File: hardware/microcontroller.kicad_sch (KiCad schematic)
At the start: 12 parts, among them J1 AVR-ISP-6, SW1 SW_Push_Open_Dual, U1 ATmega328P-A, Y1 Crystal

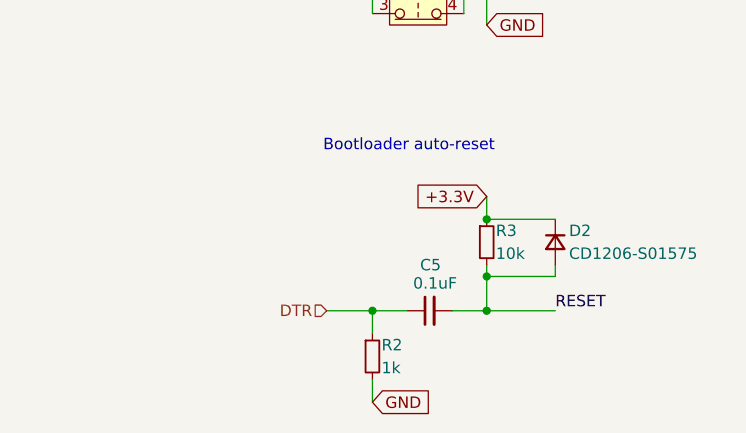
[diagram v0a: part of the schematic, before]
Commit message: Minor cosmetic changes
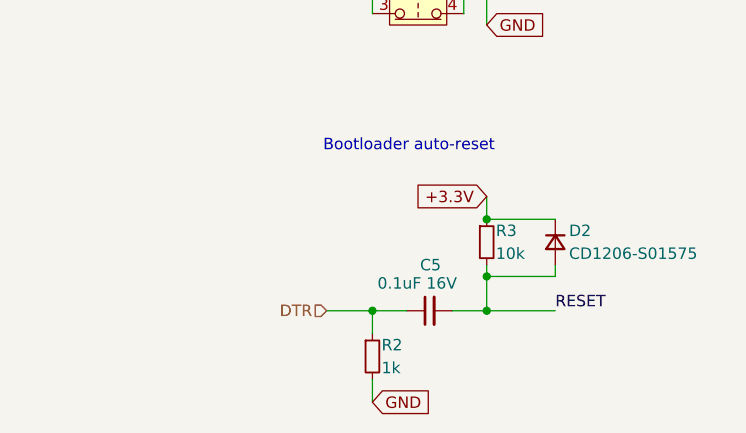
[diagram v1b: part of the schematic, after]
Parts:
- C5: value 0.1uF -> 0.1uF 16V; Package (none) -> 0805; Part Num (none) -> GRM21BR71H104KA01L; Price/unit (none) -> $0.0097; Supplier Link (none) -> https://jlcpcb.com/partdetail/MurataElectronics-GRM21BR71H1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
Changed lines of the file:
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@@
 			)
 		)
-		(property "Value" "0.1uF"
+		(property "Value" "0.1uF 16V"
 			(at 239.268 134.112 90)
 			(effects
@@
 			)
 		)
-		(property "Datasheet" "~"
+		(property "Datasheet" "https://wmsc.lcsc.com/wmsc/upload/file/pdf/v2/lcsc/2304140030_Murata-Electronics-GRM21BR71H104KA01L_C77082.pdf"
 			(at 236.22 137.16 0)
 			(effects
@@
 			(at 236.22 137.16 0)
 			(effects
+				(font
+					(size 1.27 1.27)
+				)
+				(hide yes)
+			)
+		)
+		(property "Package" "0805"
+			(at 236.22 137.16 0)
+			(effects
+				(font
+					(size 1.27 1.27)
+				)
+				(hide yes)
+			)
+		)
+		(property "Part Num" "GRM21BR71H104KA01L"
+			(at 236.22 137.16 0)
+			(effects
+				(font
+					(size 1.27 1.27)
+				)
+				(hide yes)
+			)
+		)
+		(property "Price/unit" "$0.0097"
+			(at 236.22 137.16 0)
+			(effects
+				(font
+					(size 1.27 1.27)
+				)
+				(hide yes)
+			)
+		)
+		(property "Supplier Link" "https://jlcpcb.com/partdetail/MurataElectronics-GRM21BR71H104KA01L/C77082"
+			(at 236.22 137.16 0)
+			(effects

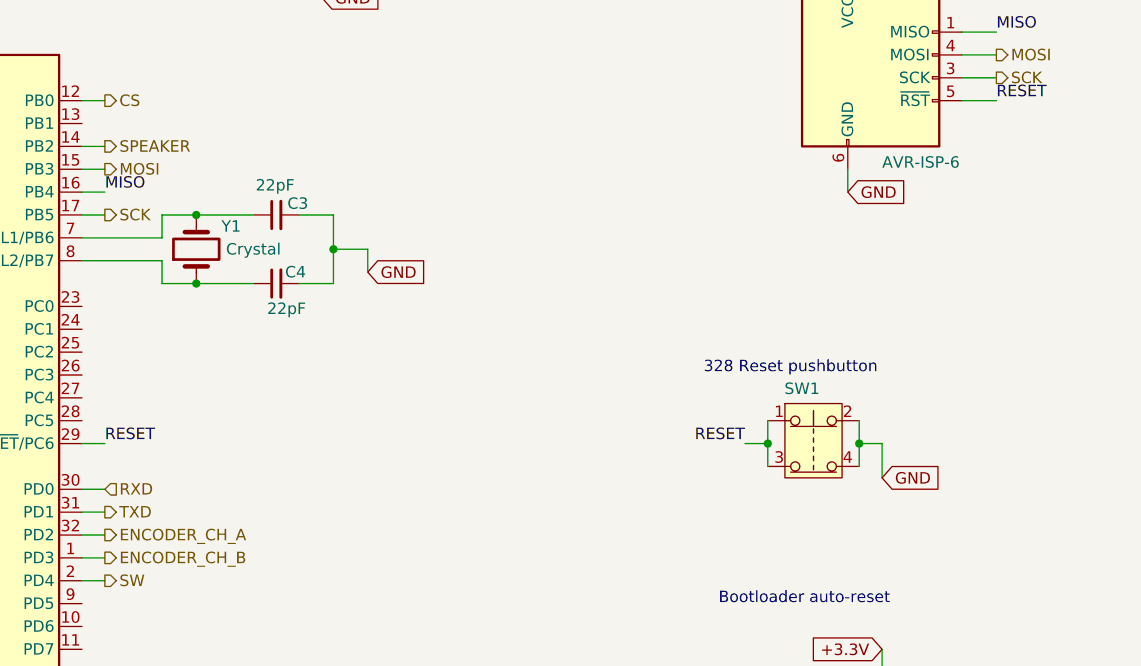
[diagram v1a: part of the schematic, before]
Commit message: Added information, footprints and 3d models for several components
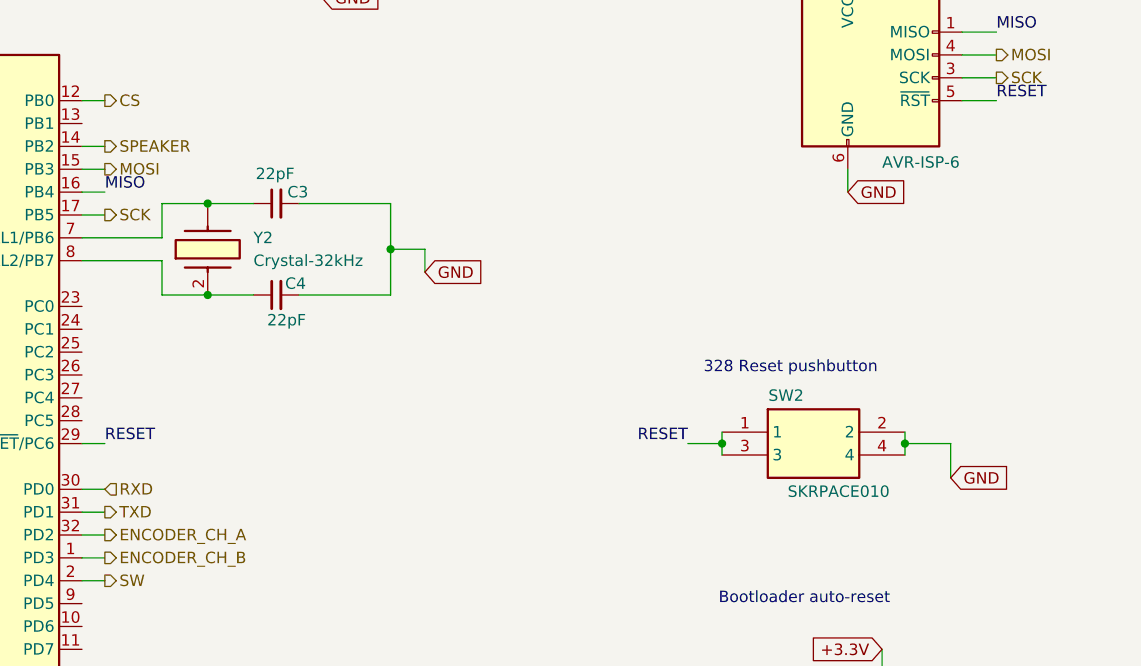
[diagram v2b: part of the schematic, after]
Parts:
- removed SW1: SW_Push_Open_Dual, symbol Switch:SW_Push_Open_Dual
- removed Y1: Crystal, symbol Device:Crystal
- added SW2: SKRPACE010, SMT(4.2X3.2), symbol kitchen_timer-symbols_lib:SKRPACE010
- added Y2: Crystal-32kHz, kitchen_timer:FL26T2-32.000, symbol kitchen_timer-symbols_lib:FL26T2-32.000
- U1: Package (none) -> TQFP-32(7x7); Part Num (none) -> ATMEGA328P-AU; Price/unit (none) -> $2.2845; Supplier Link (none) -> https://jlcpcb.com/partdetail/MicrochipTech-ATMEGA328PAU/C1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
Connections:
- net GND: now also SW2.2, SW2.4
- net RESET: now also SW2.1, SW2.3
- net at C4.1, U1.8 (XTAL2/PB7): now also Y2.2 (CRYSTAL_2)
- net at C3.1, U1.7 (XTAL1/PB6): now also Y2.
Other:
- moved on the sheet: C3, C4

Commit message: Added some information to the microcontroller sch and the power_management sch
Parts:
- SW2: Package (none) -> SMD; Part Num (none) -> SKRPACE010; Price/unit (none) -> $0.0573; Supplier Link (none) -> https://jlcpcb.com/partdetail/Alpsalpine-SKRPACE010/C139797
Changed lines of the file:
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@@
 			)
 		)
-		(property "Datasheet" "http://www.alps.com/prod/info/E/HTML/Tact/SurfaceMount/SKRP/SKRPACE010.html"
+		(property "Datasheet" "https://www.lcsc.com/datasheet/lcsc_datasheet_1811051610_ALPSALPINE-SKRPACE010_C139797.pdf"
 			(at 241.3 295.25 0)
 			(effects
@@
 				(hide yes)
 			)
+		)
+		(property "Supplier Link" "https://jlcpcb.com/partdetail/Alpsalpine-SKRPACE010/C139797"
+			(at 224.79 100.33 0)
+			(effects
+				(font
+					(size 1.27 1.27)
+				)
+				(hide yes)
+			)
+		)
+		(property "Price/unit" " $0.0573"
+			(at 224.79 100.33 0)
+			(effects
+				(font
+					(size 1.27 1.27)
+				)
+				(hide yes)
+			)
+		)
+		(property "Part Num" "SKRPACE010"
+			(at 224.79 100.33 0)
+			(effects
+				(font
+					(size 1.27 1.27)
+				)
+				(hide yes)
+			)
+		)
+		(property "Package" "SMD"
+			(at 224.79 100.33 0)
+			(effects
+				(font
+					(size 1.27 1.27)
+				)
+				(hide yes)
+			)

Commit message: Added TP4056 footprint andconfirmed components in UART and BMS schematics.
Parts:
- SW2: footprint SMT(4.2X3.2) -> (none)
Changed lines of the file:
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@@
 			)
 		)
-		(property "Footprint" "SMT(4.2X3.2)"
+		(property "Footprint" ""
 			(at 241.3 195.25 0)
 			(effects

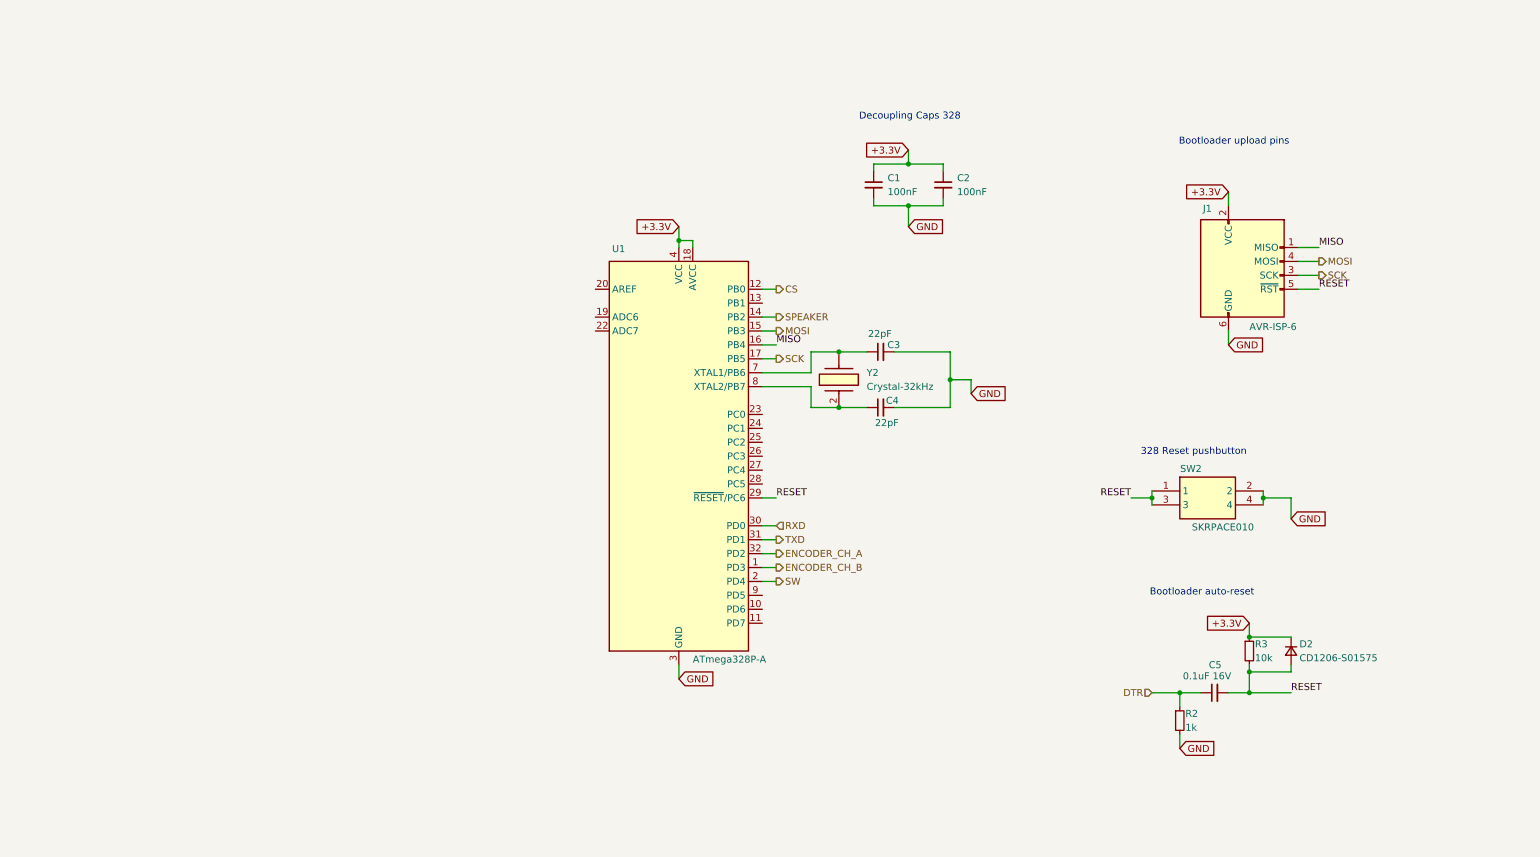
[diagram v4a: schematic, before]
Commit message: Removed the 3.3V Regulator since we might need to run everything out of 5V
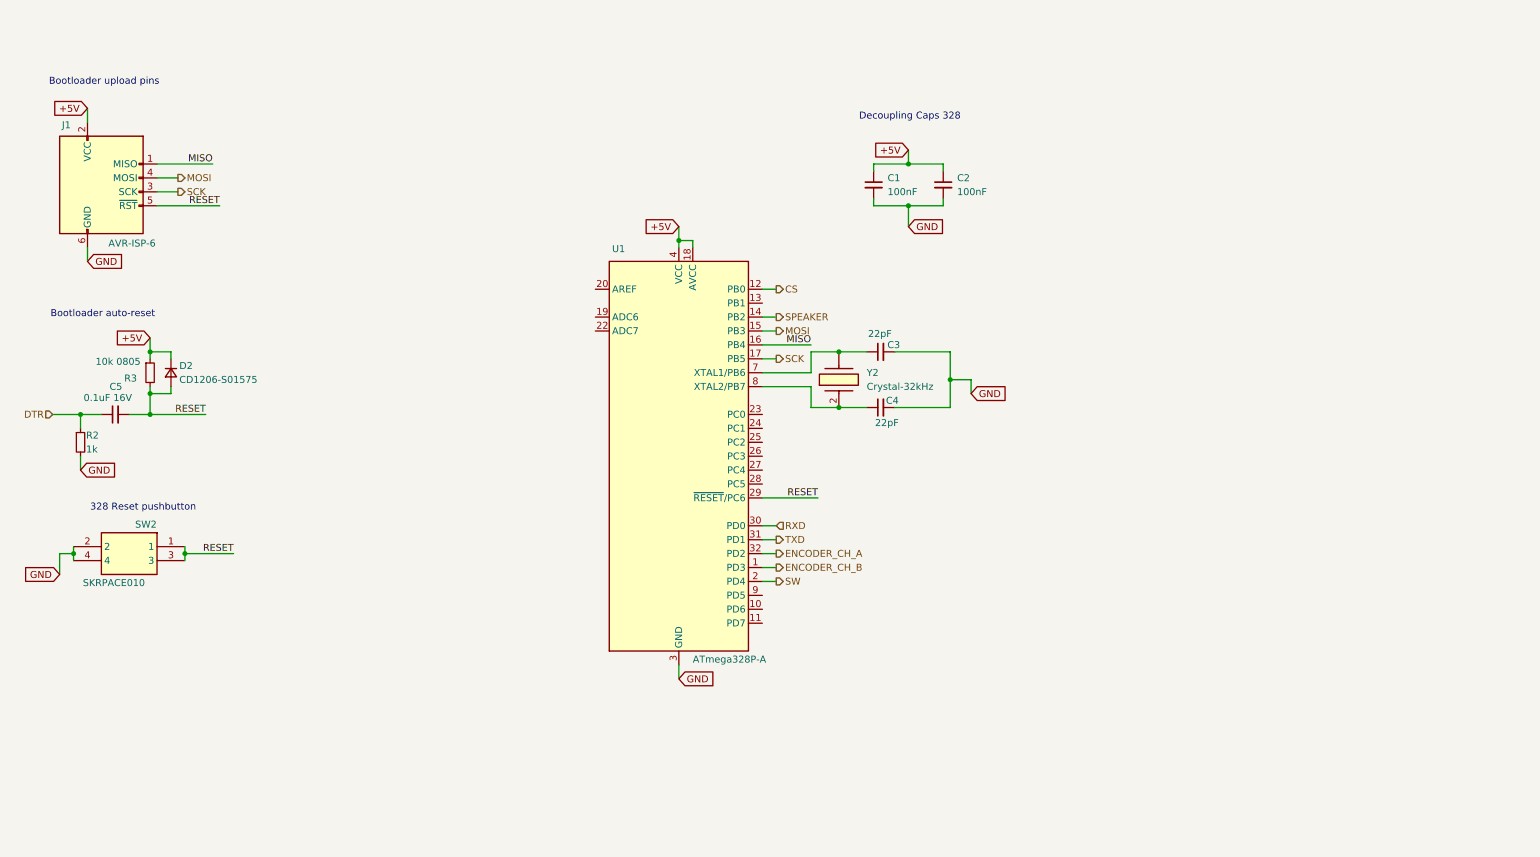
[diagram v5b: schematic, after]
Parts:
- R3: value 10k -> 10k 0805; Package (none) -> 0805; Part Num (none) -> 0805W8F1002T5E; Price/unit (none) -> $0.0017; Supplier Link (none) -> https://jlcpcb.com/partdetail/18102-0805W8F1002T5E/C17414
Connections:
- net +3.3V renamed +5V
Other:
- moved on the sheet: C5, D2, J1, R2, SW2

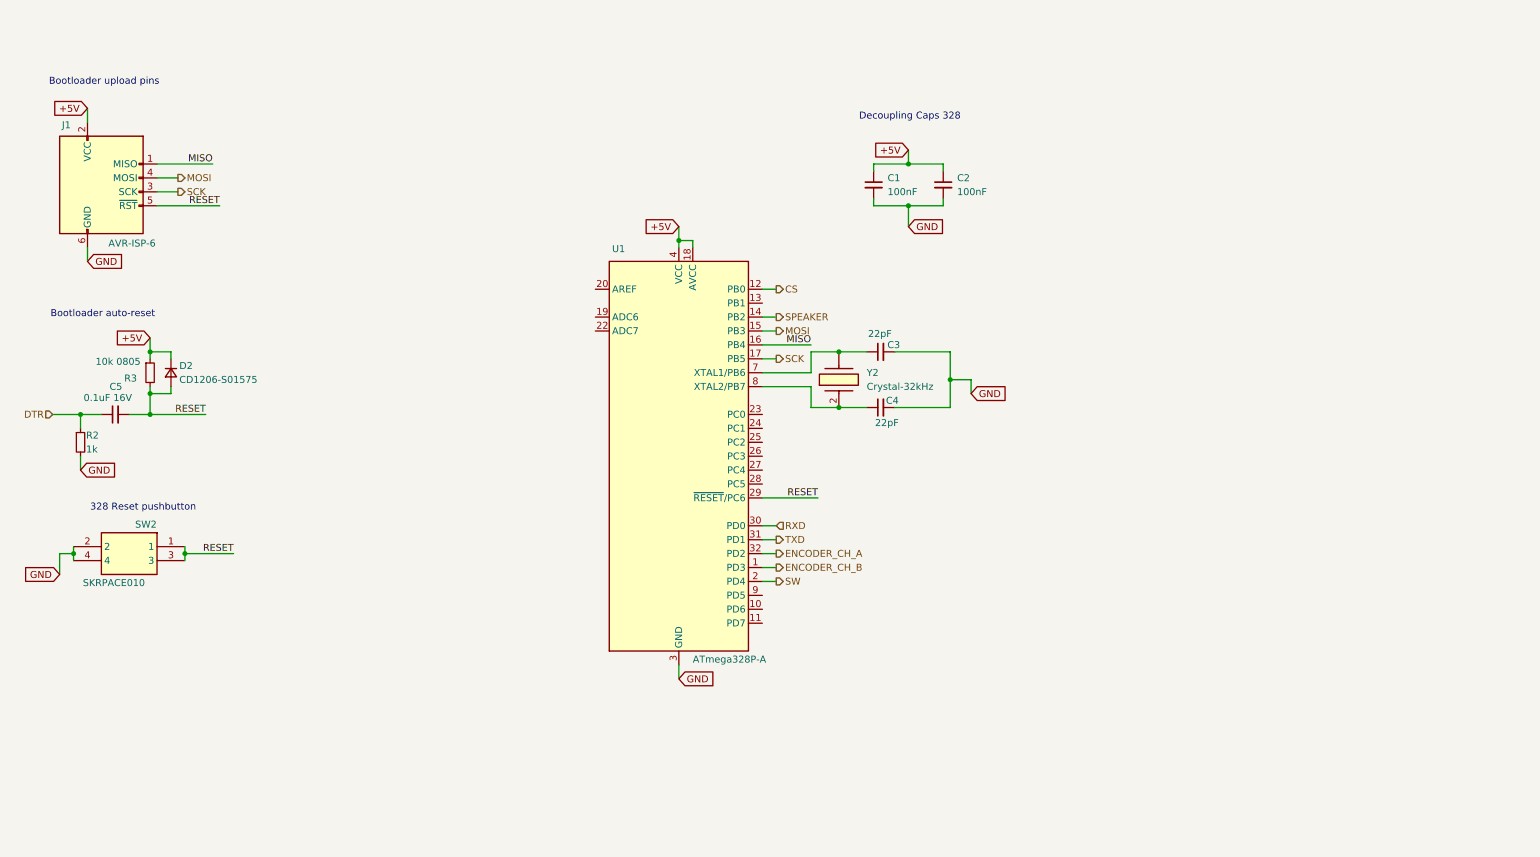
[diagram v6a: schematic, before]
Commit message: Schematic completed, commented and ready for review
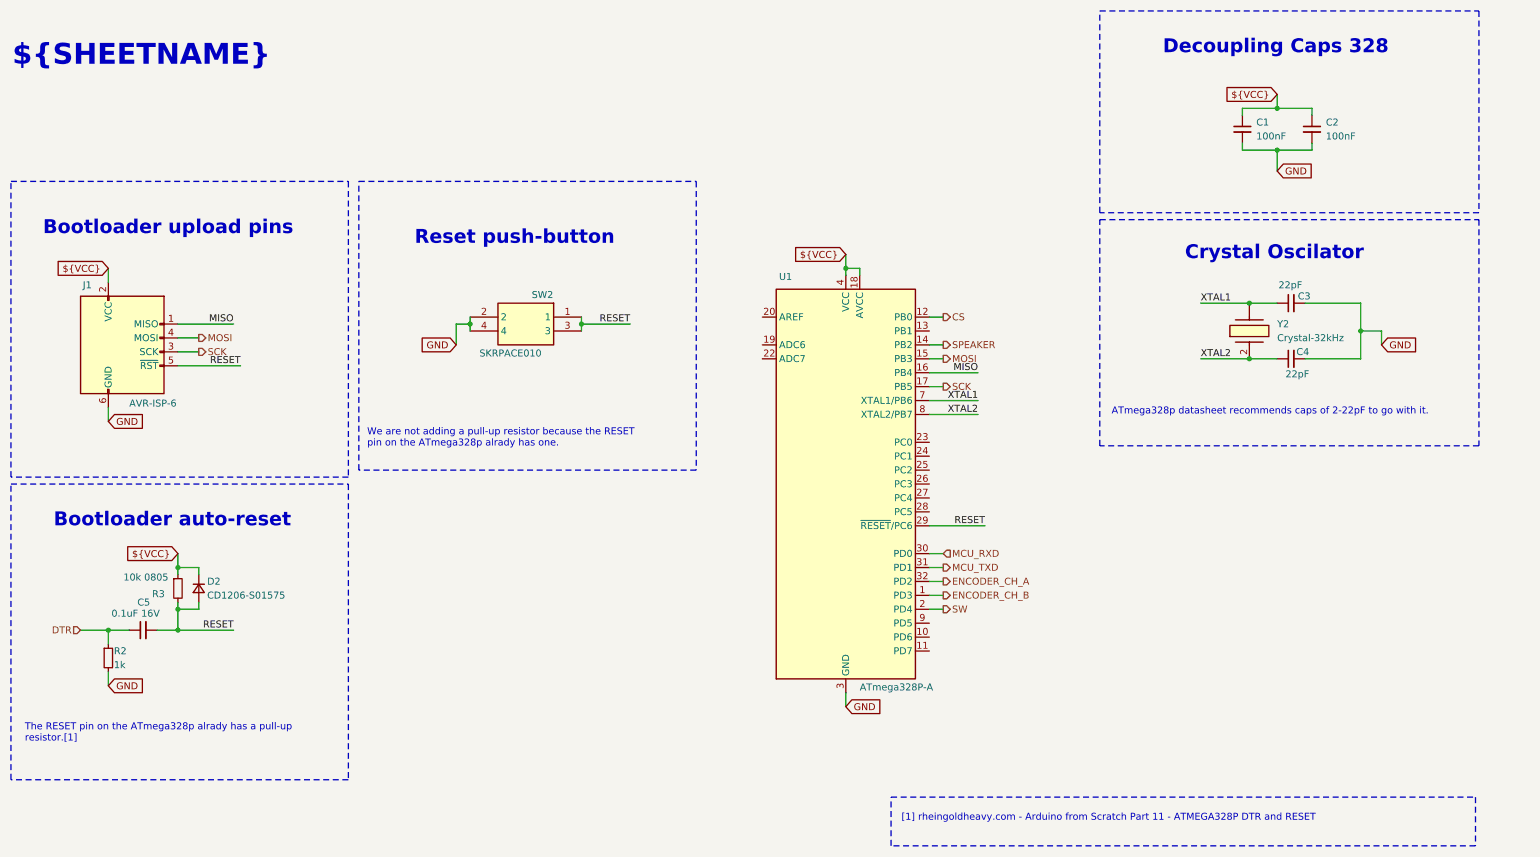
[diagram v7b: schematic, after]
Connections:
- net XTAL1: now reaches C3.1, U1.7 (XTAL1/PB6), Y2.
- net XTAL2: now reaches C4.1, U1.8 (XTAL2/PB7), Y2.2 (CRYSTAL_2)
- net +5V renamed ${VCC}
- net RXD renamed MCU_RXD
- net TXD renamed MCU_TXD
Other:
- note added: "${SHEETNAME}"
- note added: "ATmega328p datasheet recommends caps of 2-22pF to go with it."
- note added: "Crystal Oscilator"
- note added: "Reset push-button"
- note added: "The RESET pin on the ATmega328p alrady has a pull-up resistor.[1]"
- note added: "We are not adding a pull-up resistor because the RESET pin on the ATmega328p alrady has one."
- note added: "[1] rheingoldheavy.com - Arduino from Scratch Part 11 - ATMEGA328P DTR and RESET"
- note removed: "328 Reset pushbutton"
- title: Kitchen_Timer - Microcontroller -> Kitchen_Timer - ${SHEETNAME}
- moved on the sheet: C1, C2, C3, C4, C5, D2, J1, R2, R3, SW2, U1, Y2
